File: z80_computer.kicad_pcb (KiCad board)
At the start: 2 copper layers, 13 parts, among them J7 CompactFlash Port, U12 Z84C40-SIO-0, U24 OPEN-SMART-3.5

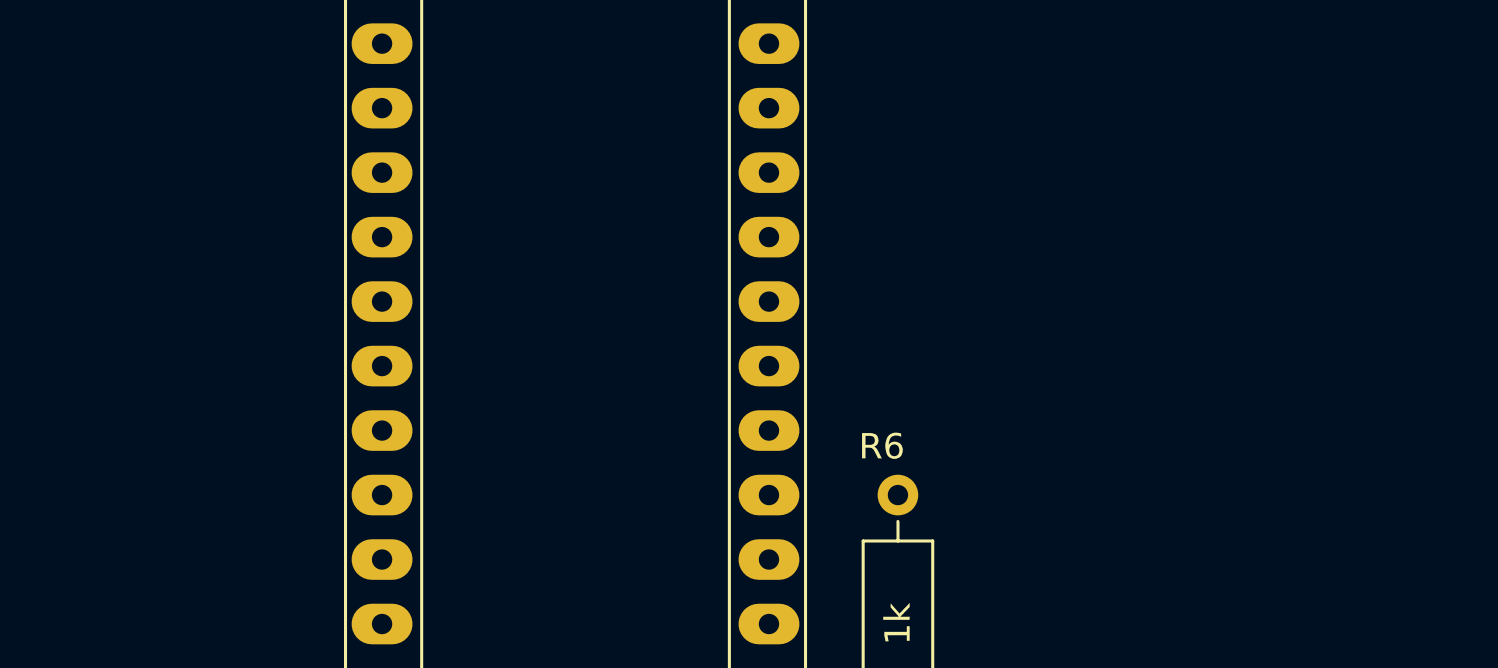
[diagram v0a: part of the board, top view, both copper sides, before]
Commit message: Added two pullups to SIO/SYNC
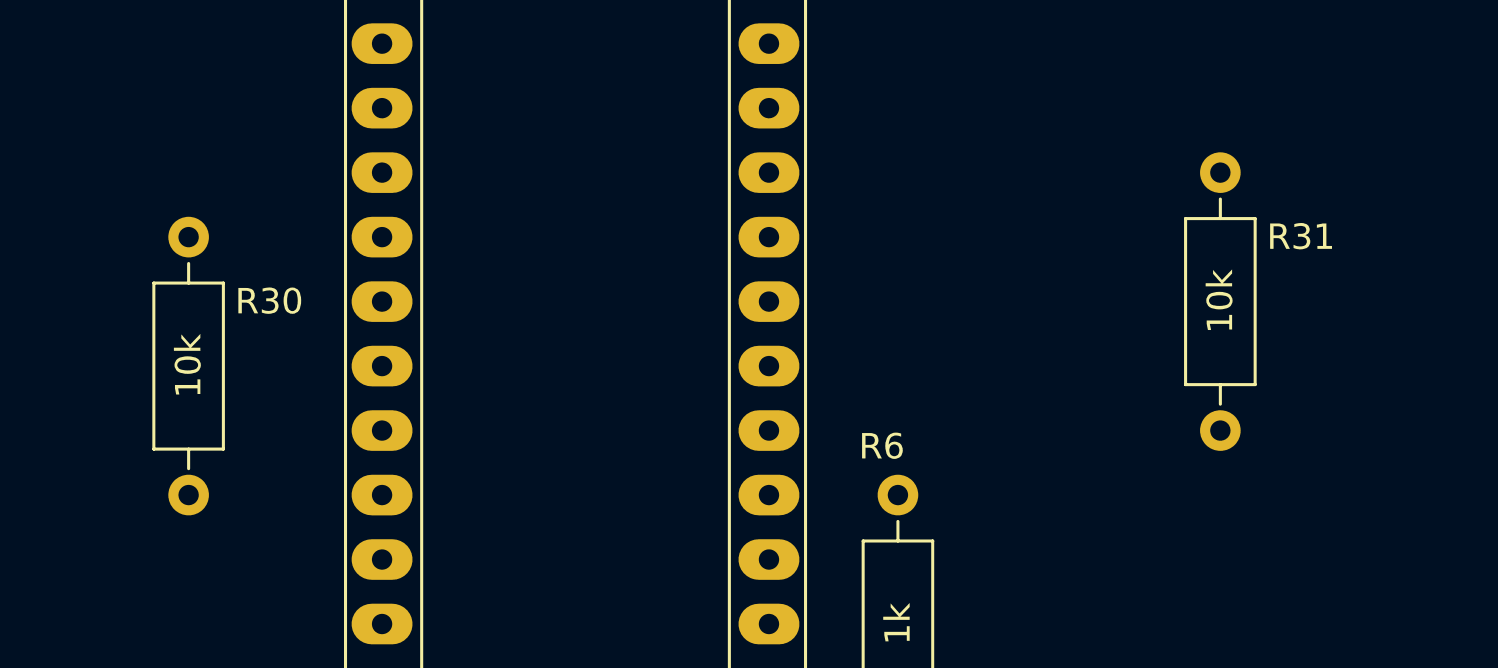
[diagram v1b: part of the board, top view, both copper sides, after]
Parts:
- added R30: 10k, Resistor_THT:R_Axial_DIN0207_L6.3mm_D2.5mm_P10.16mm_Horizontal, F.Cu at (255.3, 157.5)
- added R31: 10k, Resistor_THT:R_Axial_DIN0207_L6.3mm_D2.5mm_P10.16mm_Horizontal, F.Cu at (295.9, 154.9)
